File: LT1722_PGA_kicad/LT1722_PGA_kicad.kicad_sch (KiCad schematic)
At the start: 31 parts, among them U1 LT1722, U2 LT1722, U3 ${SIM.PARAMS}

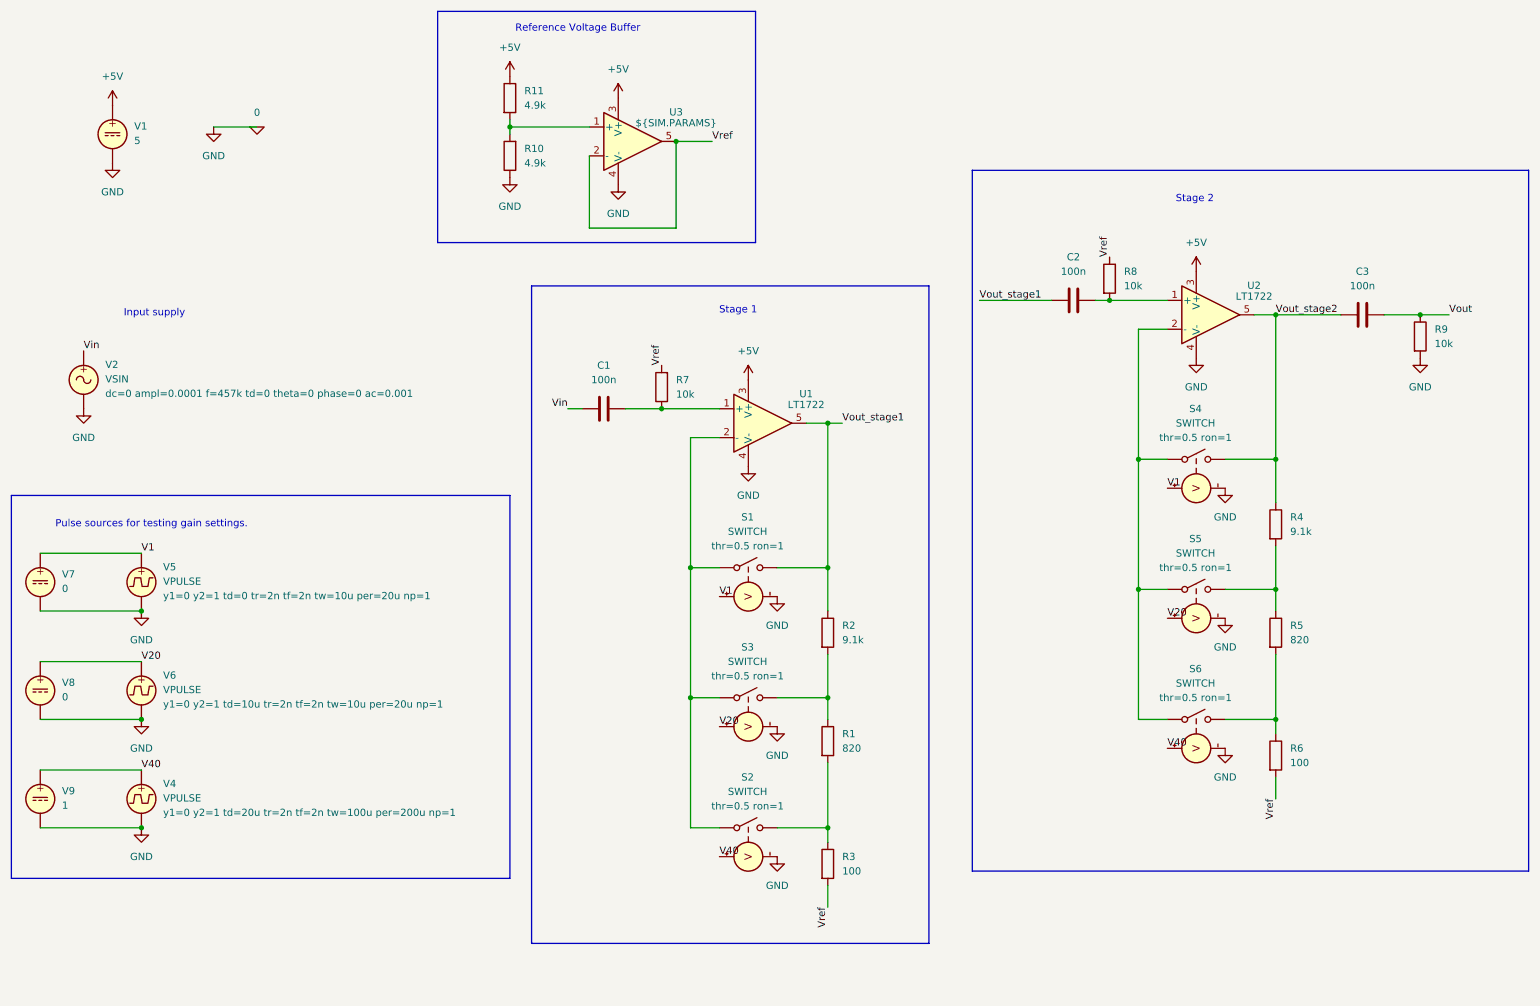
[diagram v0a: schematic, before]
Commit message: reimplemented with inverting PGA intended for use with a potentiometer, and a first stage that two settings (high gain, unity gain)
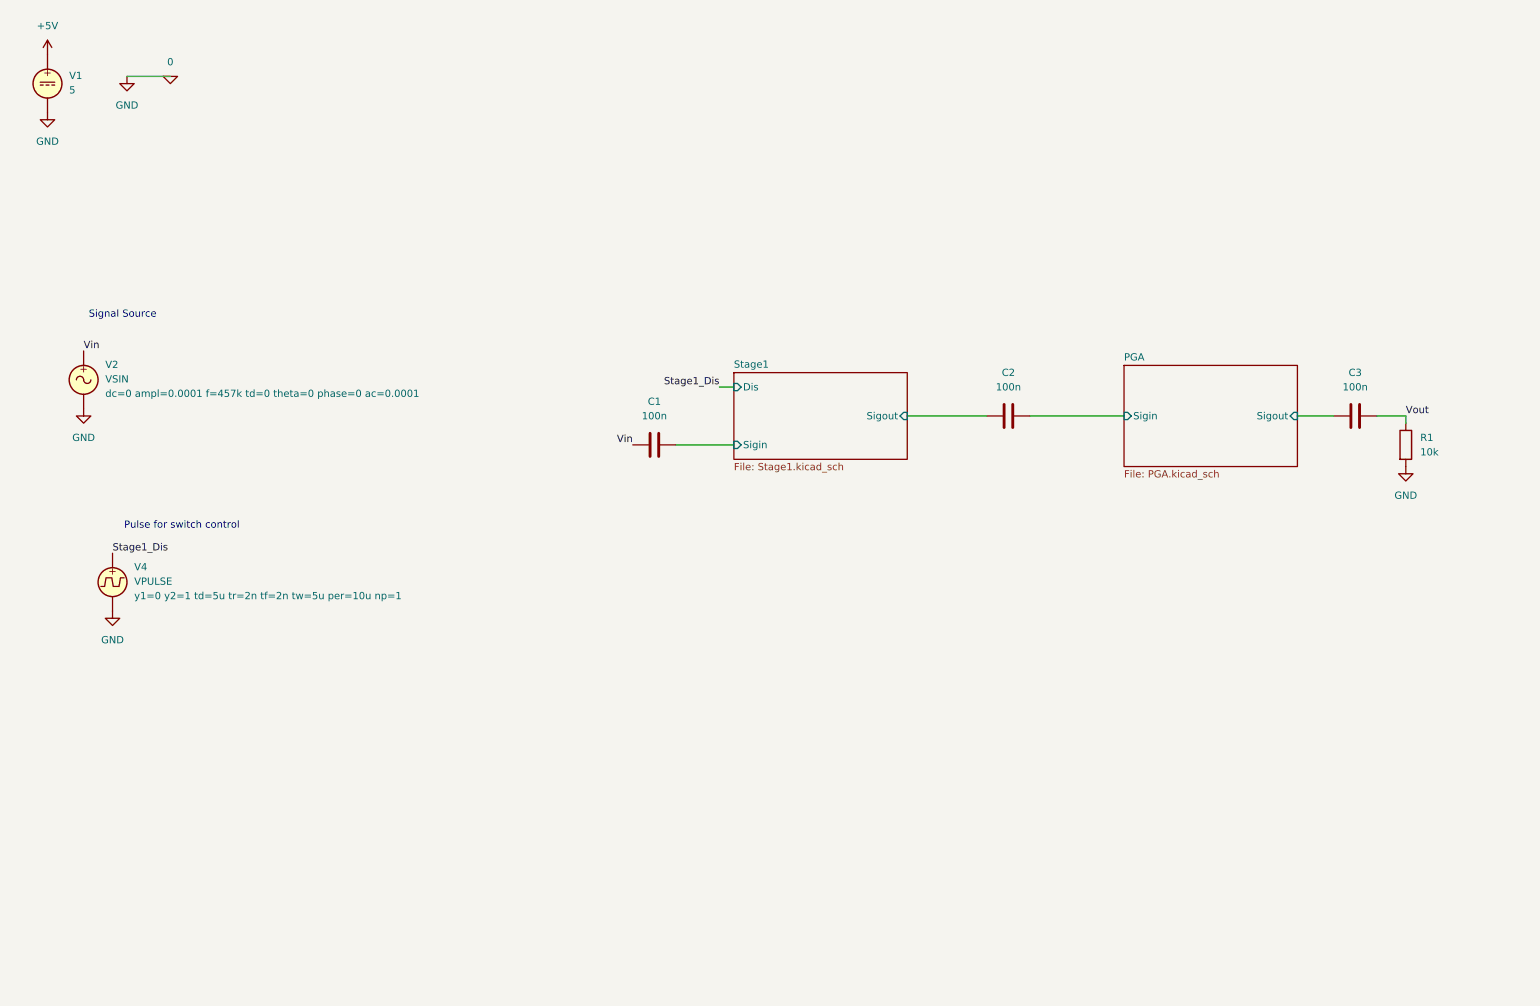
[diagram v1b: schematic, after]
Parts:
- removed R10, R11: 4.9k, symbol Device:R
- removed R2, R4: 9.1k, symbol Device:R
- removed R3, R6: 100, symbol Device:R
- removed R5: 820, symbol Device:R
- removed R7, R8, R9: 10k, symbol Device:R
- removed S1, S2, S3, S4, S5, S6: SWITCH, symbol Simulation_SPICE:SWITCH
- removed U1, U2: LT1722, symbol Simulation_SPICE:OPAMP
- removed U3: ${SIM.PARAMS}, symbol Simulation_SPICE:OPAMP
- removed V5, V6: VPULSE, symbol Simulation_SPICE:VPULSE
- removed V7, V8: 0, symbol Simulation_SPICE:VDC
- removed V9: 1, symbol Simulation_SPICE:VDC
- R1: value 820 -> 10k
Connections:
- net 0: now also R1.2
- net Vout: now also R1.1
- net PGA/Sigin: now reaches C2.2
- net Stage1/Sigin: now reaches C1.2
- net V40 renamed Stage1_Dis
- net Vout_stage1 renamed Stage1/Sigout
- net Vout_stage2 renamed PGA/Sigout
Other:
- added sheet PGA (PGA.kicad_sch)
- added sheet Stage1 (Stage1.kicad_sch)
- note added: "Pulse for switch control"
- note added: "Signal Source"
- note removed: "Input supply"
- note removed: "Pulse sources for testing gain settings."
- note removed: "Reference Voltage Buffer"
- note removed: "Stage 1"
- note removed: "Stage 2"
- moved on the sheet: V1

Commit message: change to bypass of first stage amplifier, add schematic for a tuned cascode
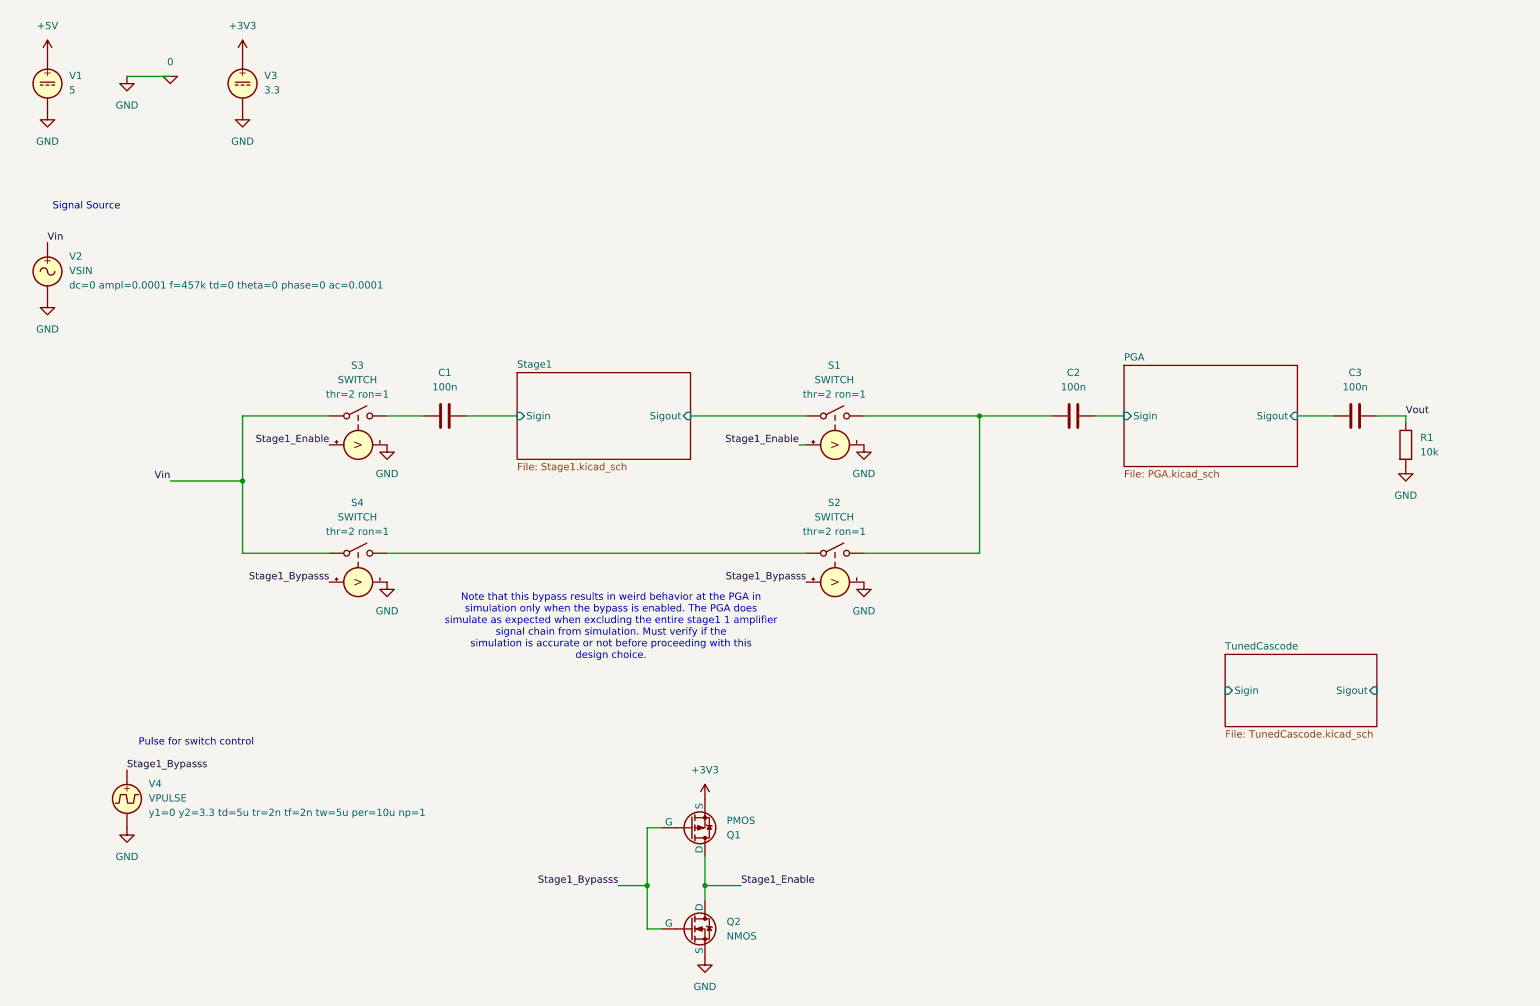
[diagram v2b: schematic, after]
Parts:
- added Q1: PMOS, symbol Simulation_SPICE:PMOS
- added Q2: NMOS, symbol Simulation_SPICE:NMOS
- added S1, S2, S3, S4: SWITCH, symbol Simulation_SPICE:SWITCH
- added V3: 3.3, symbol Simulation_SPICE:VDC
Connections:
- net 0: now also Q2.3 (S), S1.4 (C-), S2.4 (C-), S3.4 (C-), S4.4 (C-), V3.2
- net Stage1/Sigout: now also S1.1 (N+); no longer C2.1
- net Vin: now also S3.1 (N+), S4.1 (N+); no longer C1.1
- net Stage1_Dis renamed Stage1_Bypasss
- net Stage1_Bypasss: now also Q1.2 (G), Q2.2 (G), S2.3 (C+), S4.3 (C+)
- new net: C1.1, S3.2 (N-)
- new net: C2.1, S1.2 (N-), S2.2 (N-)
- new net: S2.1 (N+), S4.2 (N-)
- new net +3V3: Q1.3 (S), V3.1
- new net Stage1_Enable: Q1.1 (D), Q2.1 (D), S1.3 (C+), S3.3 (C+)
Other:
- added sheet TunedCascode (TunedCascode.kicad_sch)
- sheet Stage1 ports: added none; removed Dis
- note added: "Note that this bypass results in weird behavior at the PGA in simulation only when the bypass is enabled. The PGA does simulate as expected when excluding the entire stage1 1 amplifier signal chain from simulation. Must verify if the simulation is accurate or not before proceeding with this design choice."
- moved on the sheet: C1, C2, V2, V4

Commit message: change stage1 and pga to be tuned
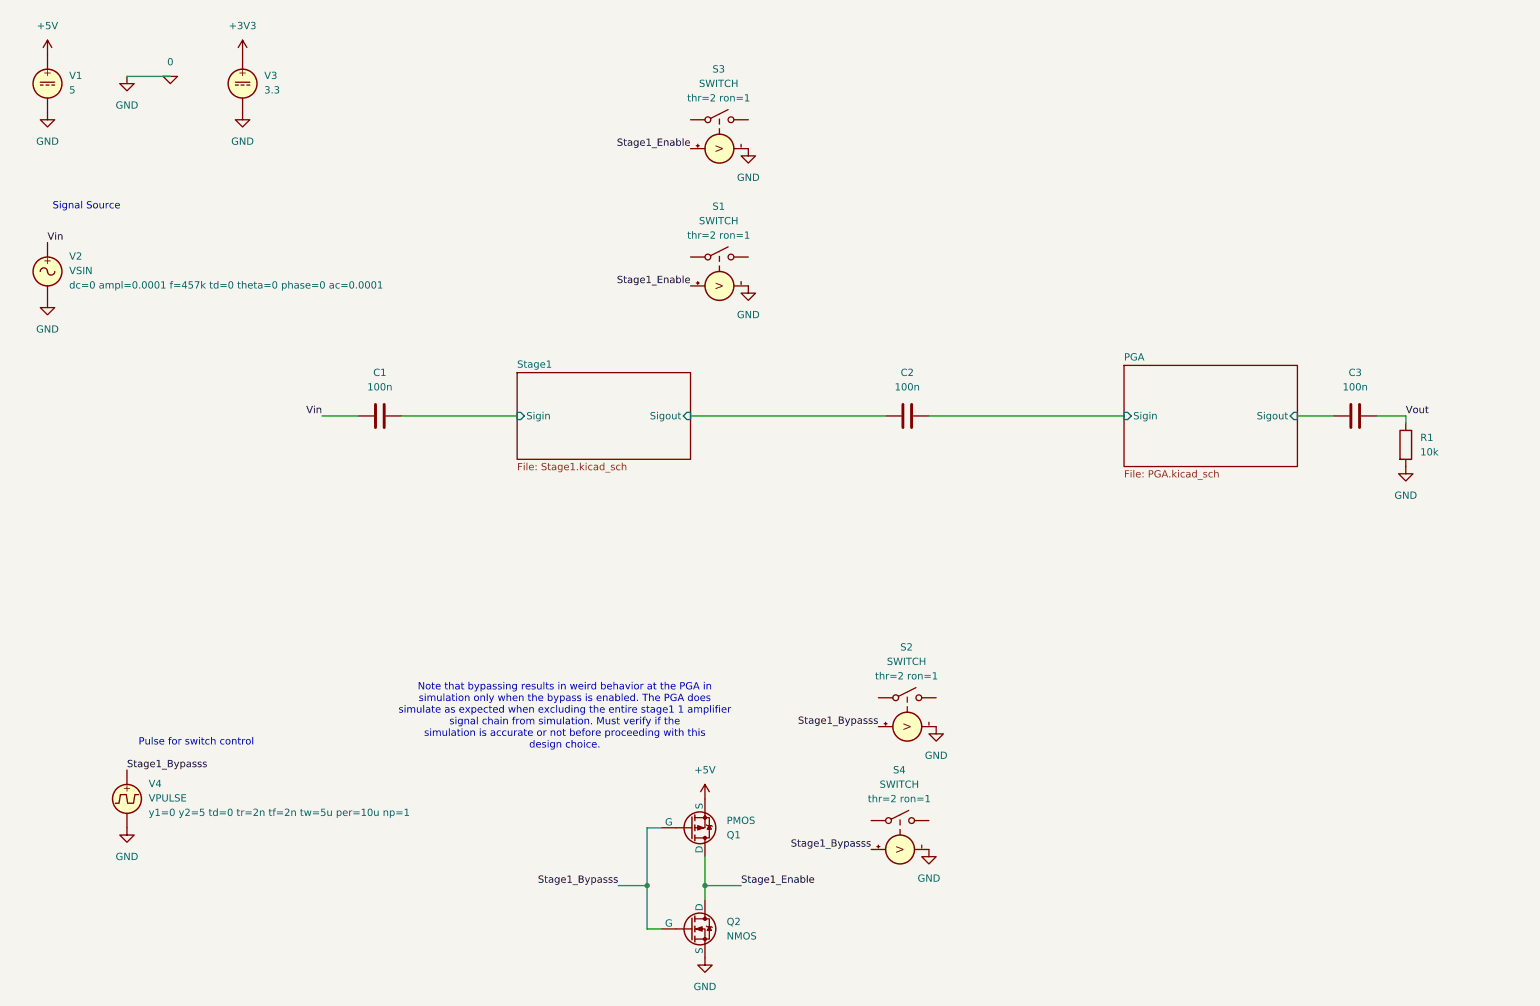
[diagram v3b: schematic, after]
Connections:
- net +3V3: no longer Q1.3 (S)
- net +5V: now also Q1.3 (S)
- net Stage1/Sigout: now also C2.1; no longer S1.1 (N+)
- net Vin: now also C1.1; no longer S3.1 (N+), S4.1 (N+)
- net at S3.2 (N-): no longer C1.1
- net at S2.1 (N+): no longer S4.2 (N-)
- now unconnected: S1.2 (N-), S2.2 (N-)
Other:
- removed sheet TunedCascode
- note added: "Note that bypassing results in weird behavior at the PGA in simulation only when the bypass is enabled. The PGA does simulate as expected when excluding the entire stage1 1 amplifier signal chain from simulation. Must verify if the simulation is accurate or not before proceeding with this design choice."
- note removed: "Note that this bypass results in weird behavior at the PGA in simulation only when the bypass is enabled. The PGA does simulate as expected when excluding the entire stage1 1 amplifier signal chain from simulation. Must verify if the simulation is accurate or not before proceeding with this design choice."
- moved on the sheet: C1, C2, S1, S2, S3, S4
